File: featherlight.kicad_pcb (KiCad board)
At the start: 4 copper layers, 50.8 x 50.8 mm, 106 parts, among them P1 USB_OTG, P11 CONN_01X06, P12 CONN_01X06, P13 CONN_01X06, P14 CONN_01X06, P15 CONN_01X06, P16 CONN_01X06, P17 CONN_01X06, P2 CONN_01X02, P3 CONN_01X01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

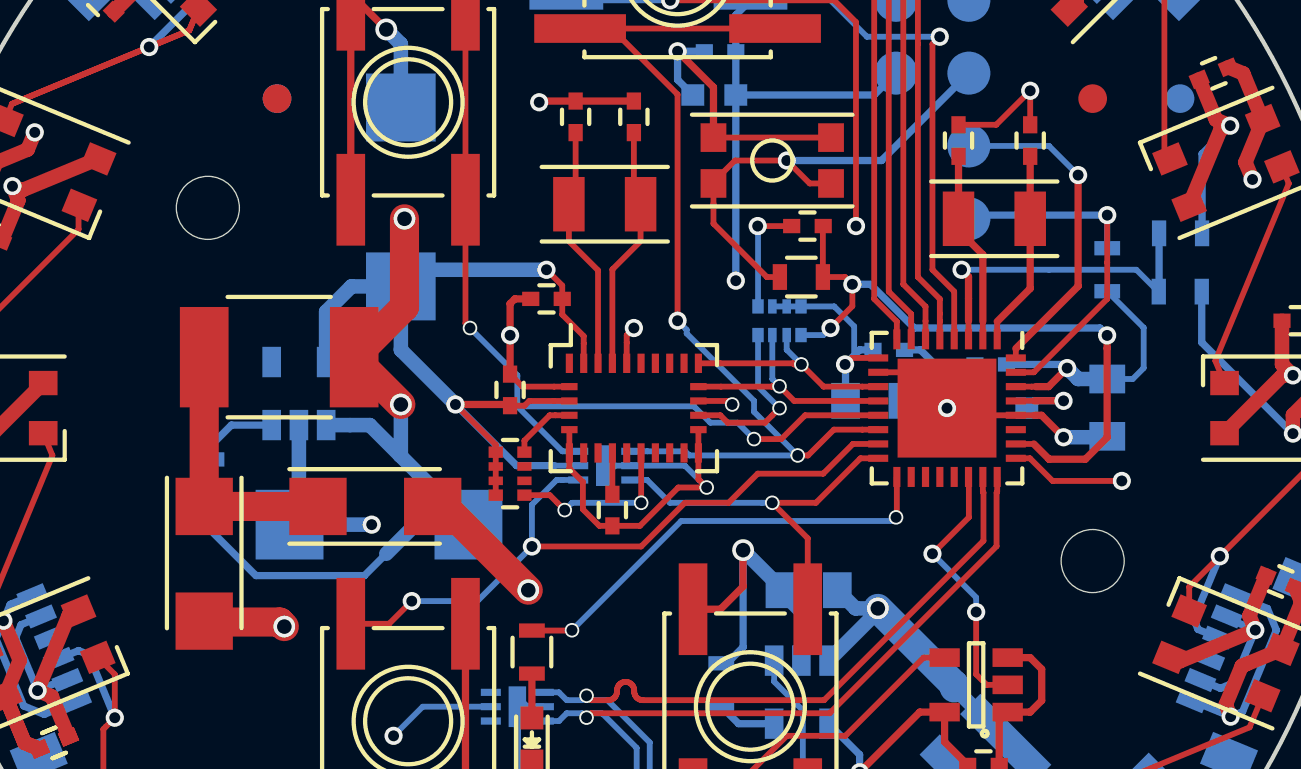
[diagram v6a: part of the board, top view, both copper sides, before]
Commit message: Bumped mounting holes up to M2.5 (Adafruit again).
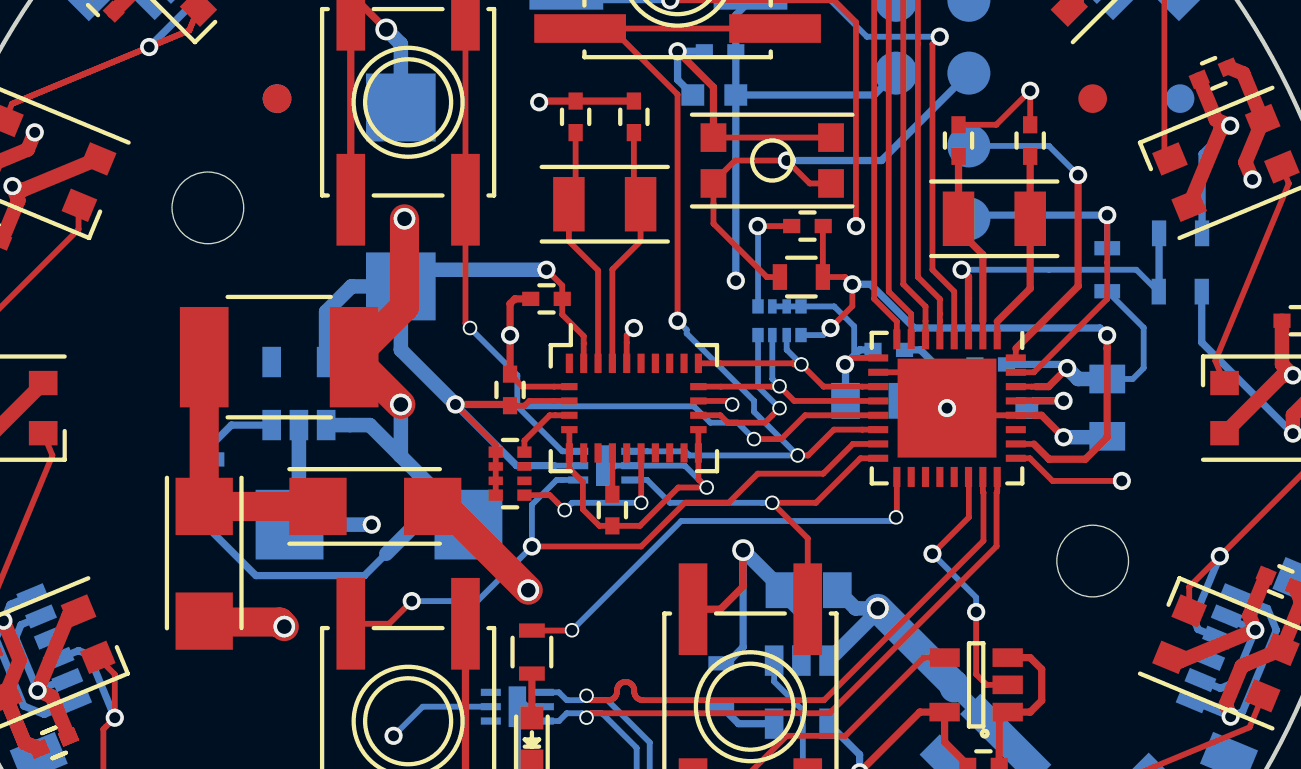
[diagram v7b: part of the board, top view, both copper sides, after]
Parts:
- HOLE1, HOLE2: footprint Mounting_Holes:MountingHole_2.2mm_M2 -> Mounting_Holes:MountingHole_2.5mm
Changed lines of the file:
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@@
-(kicad_pcb (version 20160815) (host pcbnew no-vcs-found-7444~57~ubuntu16.10.1)
+(kicad_pcb (version 20160815) (host pcbnew no-vcs-found-7448~57~ubuntu16.10.1)
   (general
     (links 278)
     (no_connects 2)
-    (area 62.814286 74.542819 139.623716 137.492001)
+    (area 76.124999 76.124999 127.075001 127.075001)
     (thickness 1.6002)
     (drawings 91)
@@
   )
   (setup
-    (last_trace_width 1.016)
+    (last_trace_width 0.1778)
     (user_trace_width 0.1778)
     (user_trace_width 0.2032)
@@
     )
   )
-  (module Mounting_Holes:MountingHole_2.2mm_M2 (layer F.Cu)
-    (at 117.602 106.934)
-    (descr "Mounting Hole 2.2mm, no annular, M2")
-    (tags "mounting hole 2.2mm no annular m2")
-    (fp_text reference HOLE2 (at 0 -3.2) (layer F.SilkS) hide
-      (effects (font (size 1 1) (thickness 0.15)))
-    )
-    (fp_text value Fiducial (at 0 3.2) (layer F.Fab)
-      (effects (font (size 1 1) (thickness 0.15)))
-    )
-    (fp_circle (center 0 0) (end 2.2 0) (layer Cmts.User) (width 0.15))
-    (fp_circle (center 0 0) (end 2.45 0) (layer F.CrtYd) (width 0.05))
-    (pad 1 np_thru_hole circle (at 0 0) (size 2.2 2.2) (drill 2.2) (layers *.Cu *.Mask))
-  )
-  (module Mounting_Holes:MountingHole_2.2mm_M2 (layer F.Cu)
-    (at 86.741 94.615)
-    (descr "Mounting Hole 2.2mm, no annular, M2")
-    (tags "mounting hole 2.2mm no annular m2")
-    (fp_text reference HOLE1 (at 0 -3.2) (layer F.SilkS) hide
-      (effects (font (size 1 1) (thickness 0.15)))
-    )
-    (fp_text value Fiducial (at 0 3.2) (layer F.Fab)
-      (effects (font (size 1 1) (thickness 0.15)))
-    )
-    (fp_circle (center 0 0) (end 2.2 0) (layer Cmts.User) (width 0.15))
-    (fp_circle (center 0 0) (end 2.45 0) (layer F.CrtYd) (width 0.05))
-    (pad 1 np_thru_hole circle (at 0 0) (size 2.2 2.2) (drill 2.2) (layers *.Cu *.Mask))
-  )
   (module Adafruit:LED_SK6812MINI-PLCC4 (layer F.Cu)
     (at 80.979363 93.04626 337.5)
@@
     )
   )
+  (module Mounting_Holes:MountingHole_2.5mm (layer F.Cu)
+    (at 86.741 94.615)
+    (descr "Mounting Hole 2.5mm, no annular")
+    (tags "mounting hole 2.5mm no annular")
+    (fp_text reference HOLE1 (at 0 -3.5) (layer F.SilkS) hide
+      (effects (font (size 1 1) (thickness 0.15)))
+    )
+    (fp_text value Fiducial (at 0 3.5) (layer F.Fab)
+      (effects (font (size 1 1) (thickness 0.15)))
+    )
+    (fp_circle (center 0 0) (end 2.75 0) (layer F.CrtYd) (width 0.05))
+    (fp_circle (center 0 0) (end 2.5 0) (layer Cmts.User) (width 0.15))
+    (pad 1 np_thru_hole circle (at 0 0) (size 2.5 2.5) (drill 2.5) (layers *.Cu *.Mask))
+  )
+  (module Mounting_Holes:MountingHole_2.5mm (layer F.Cu)
+    (at 117.602 106.934)
+    (descr "Mounting Hole 2.5mm, no annular")
+    (tags "mounting hole 2.5mm no annular")
+    (fp_text reference HOLE2 (at 0 -3.5) (layer F.SilkS) hide
+      (effects (font (size 1 1) (thickness 0.15)))
+    )
+    (fp_text value Fiducial (at 0 3.5) (layer F.Fab)
+      (effects (font (size 1 1) (thickness 0.15)))
+    )
+    (fp_circle (center 0 0) (end 2.75 0) (layer F.CrtYd) (width 0.05))
+    (fp_circle (center 0 0) (end 2.5 0) (layer Cmts.User) (width 0.15))
+    (pad 1 np_thru_hole circle (at 0 0) (size 2.5 2.5) (drill 2.5) (layers *.Cu *.Mask))
+  )
   (gr_line (start 112.268 86.36) (end 113.792 87.884) (layer Eco2.User) (width 0.2))
